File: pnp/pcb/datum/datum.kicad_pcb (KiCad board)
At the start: 2 copper layers, 80 x 35 mm, 9 parts

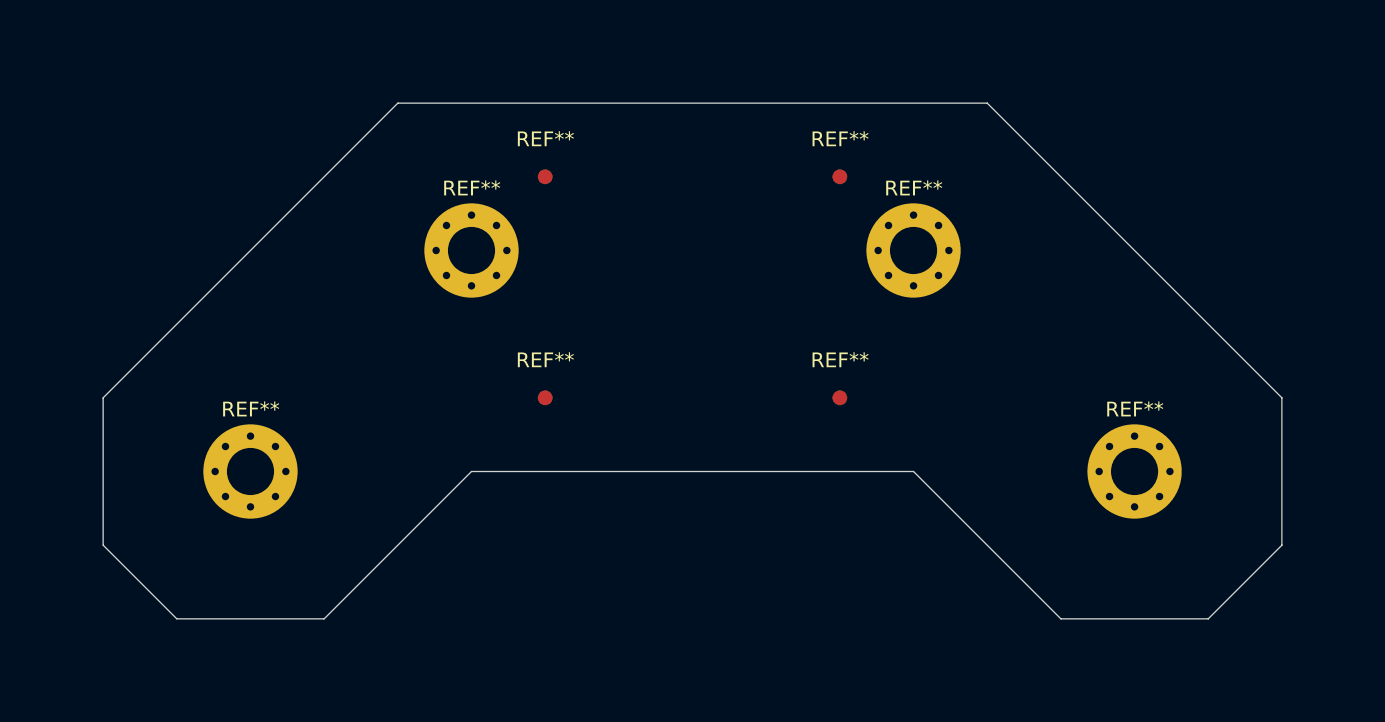
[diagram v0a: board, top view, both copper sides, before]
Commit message: got most of the top layer fids and features added
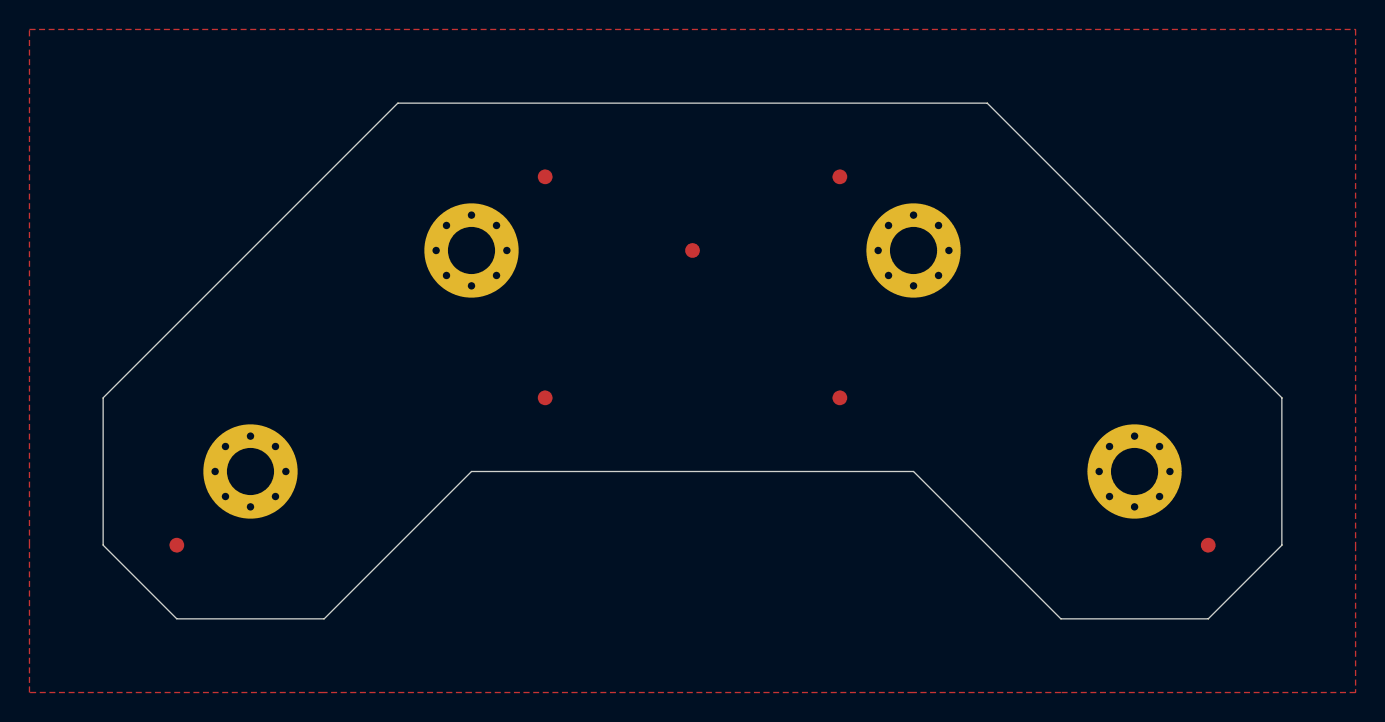
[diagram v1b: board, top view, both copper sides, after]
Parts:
- removed the REF** at (25.0, -25.0)
- removed the REF** at (55.0, -25.0)
- removed the REF** at (70.0, -10.0)
- removed the REF** at (10.0, -10.0)
- added H1: MountingHole_Pad, MountingHole:MountingHole_3.2mm_M3_Pad_Via, F.Cu at (25.0, -25.0)
- added H2: MountingHole_Pad, MountingHole:MountingHole_3.2mm_M3_Pad_Via, F.Cu at (10.0, -10.0)
- added H3: MountingHole_Pad, MountingHole:MountingHole_3.2mm_M3_Pad_Via, F.Cu at (70.0, -10.0)
- added H4: MountingHole_Pad, MountingHole:MountingHole_3.2mm_M3_Pad_Via, F.Cu at (55.0, -25.0)
- added REF**: Fiducial_1mm_Mask3mm, Fiducial:Fiducial_1mm_Mask3mm, F.Cu at (75.0, -5.00)
- added REF**: Fiducial_1mm_Mask3mm, Fiducial:Fiducial_1mm_Mask3mm, F.Cu at (5.00, -5.00)
- added REF**: Fiducial_1mm_Mask2mm, Fiducial:Fiducial_1mm_Mask2mm, F.Cu at (40.0, -25.0)
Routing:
- added copper zone on F.Cu, net GND

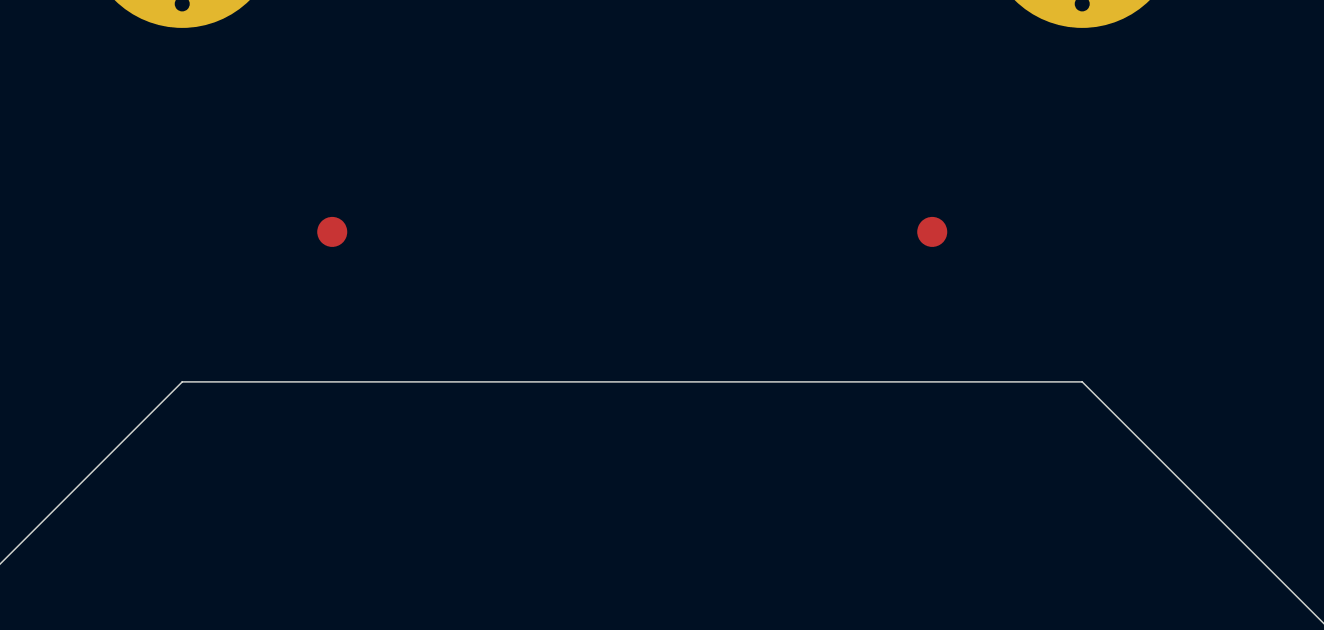
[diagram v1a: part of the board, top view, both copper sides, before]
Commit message: added footprints for ruler and dot grid for cam calibration, finalized board
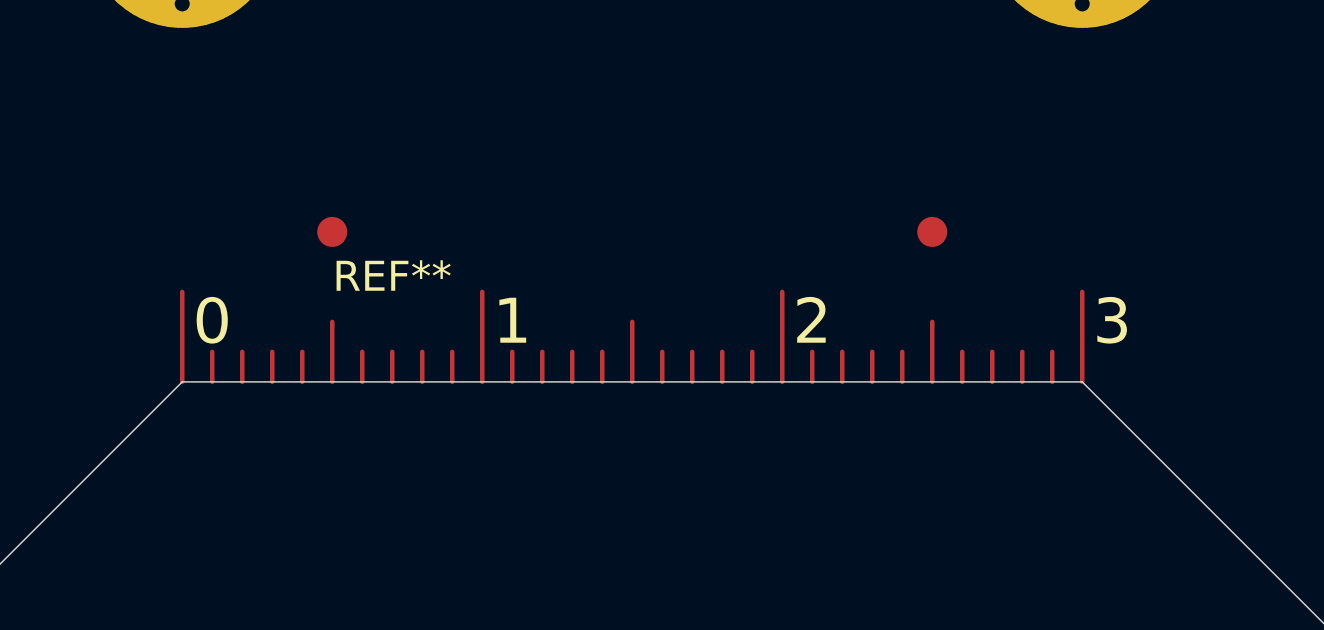
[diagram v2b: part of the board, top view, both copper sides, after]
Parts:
- added G***: LOGO, index:goblin, B.Cu at (17.0, -17.0)
- added G***: LOGO, index:cal-dot-grid, B.Cu at (40.0, -22.5)
- added REF**: Metric_Ruler_90mm, index:30mm-ruler, F.Cu at (25.0, -10.0)

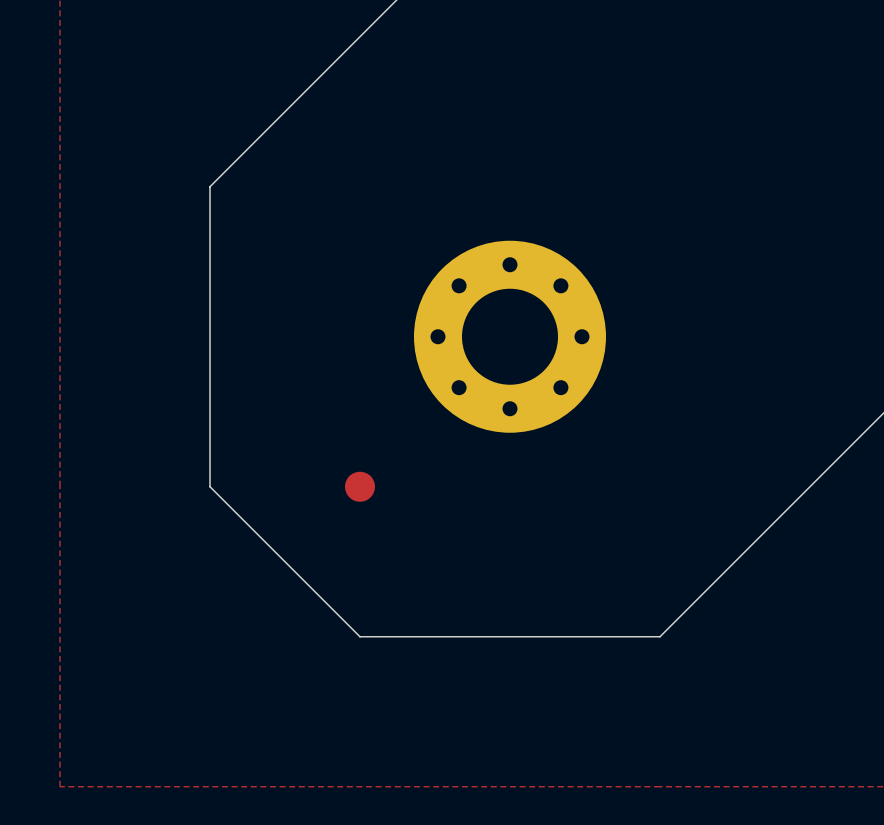
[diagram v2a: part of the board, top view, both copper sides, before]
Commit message: added castellated edges, and user drawing notes about them, along with notes about where to put the lot number
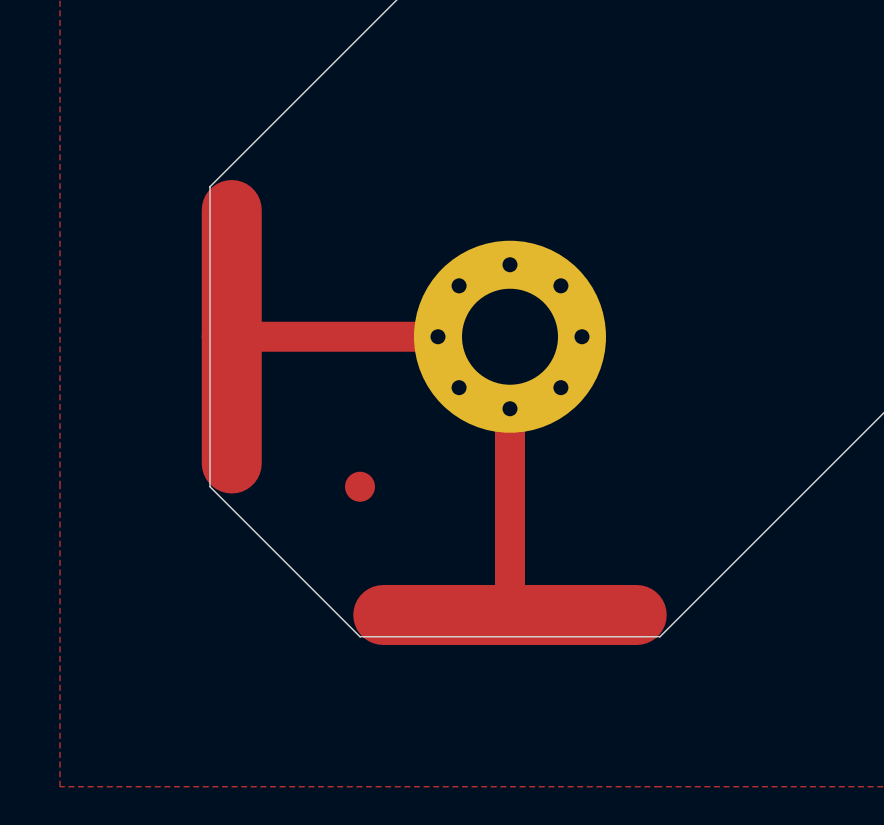
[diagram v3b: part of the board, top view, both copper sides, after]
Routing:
- net GND: track 0.00 -> 35.5 mm
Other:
- board text added: "Castellated along this flat edge"
- board text added: "Lot Number Here On Back Silkscreen"

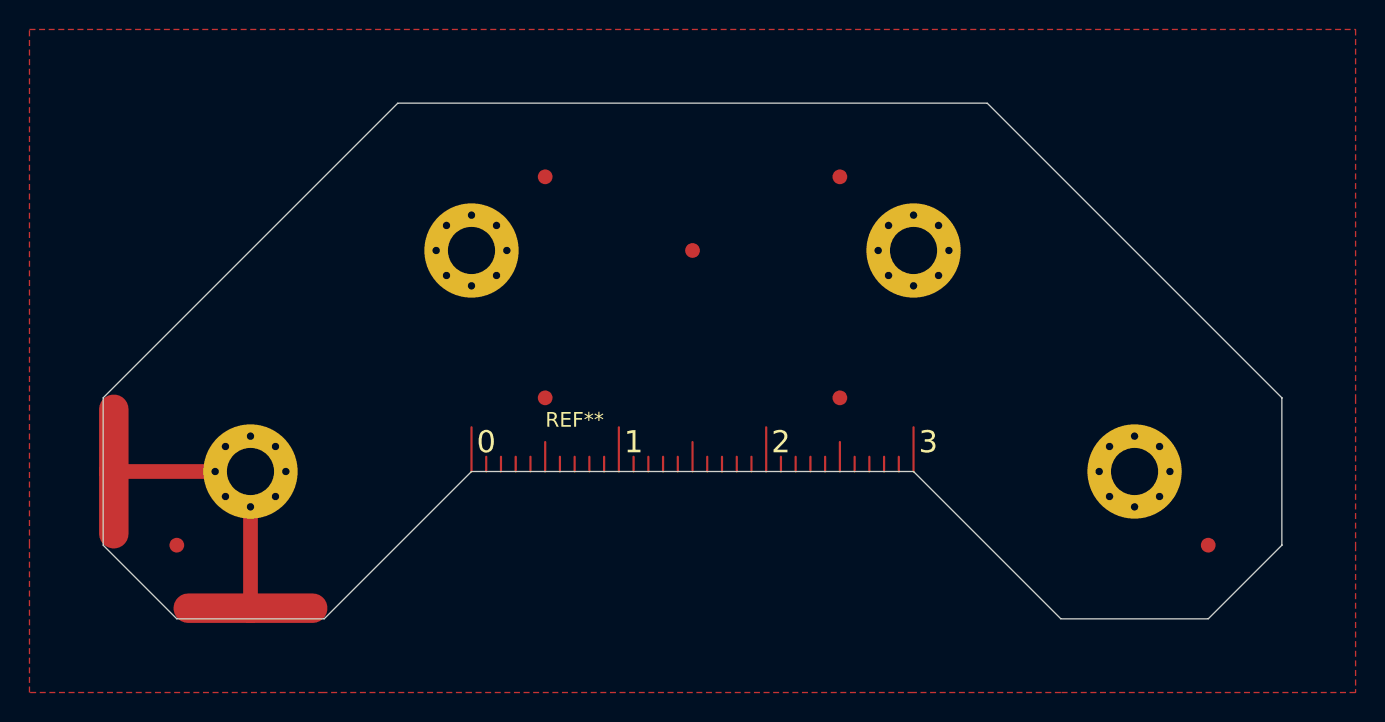
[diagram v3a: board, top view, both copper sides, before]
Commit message: made edge plating on the two internal diagonal faces, made solderable grounding pad on bottom face
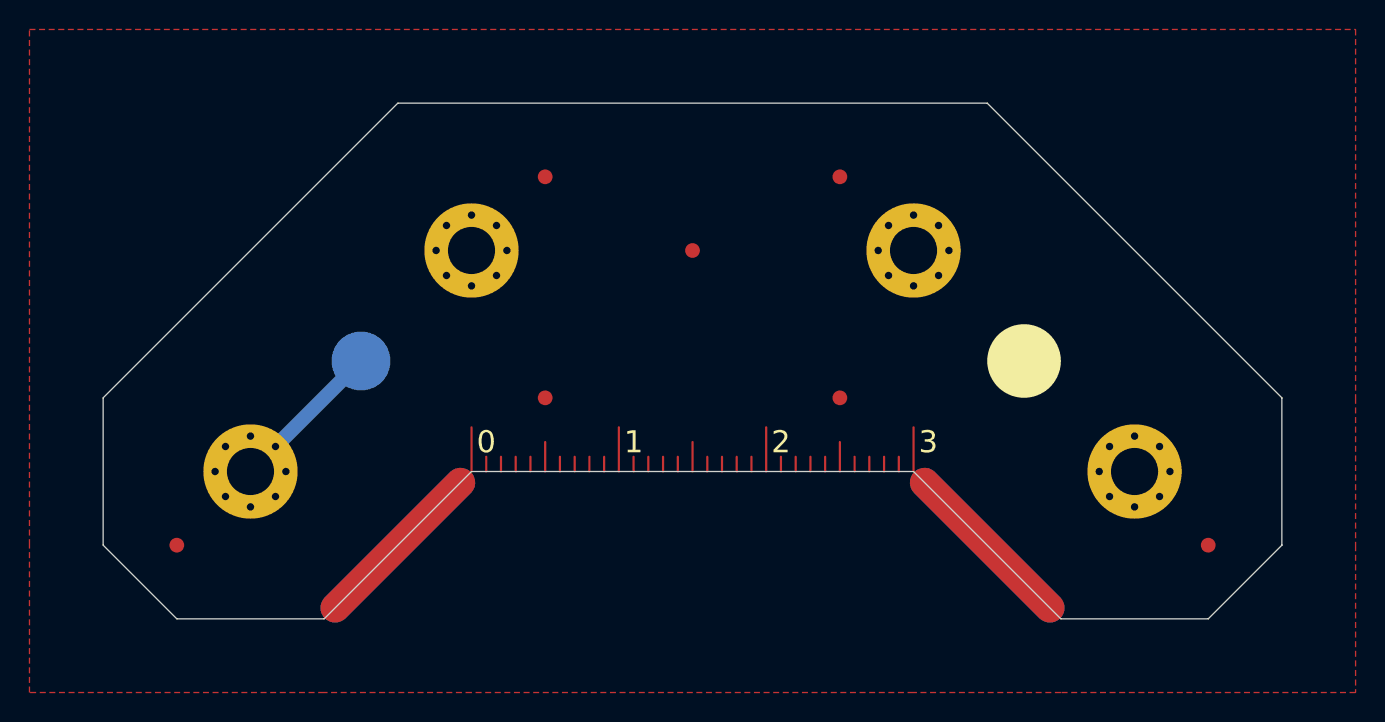
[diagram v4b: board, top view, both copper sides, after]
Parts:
- added TP1: TestPoint, TestPoint:TestPoint_Pad_D4.0mm, B.Cu at (17.5, -17.5)
- moved G*** 46.0 mm to (63.0, -17.0)
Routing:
- net (no net): track 0.00 -> 24.0 mm
- net GND: track 35.5 -> 34.6 mm
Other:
- board text added: "Plated along this flat edge"
- board text removed: "Castellated along this flat edge"
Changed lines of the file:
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@@
     (thickness 1.6)
     (drawings 33)
-    (tracks 6)
+    (tracks 5)
     (zones 0)
-    (modules 15)
+    (modules 16)
     (nets 2)
   )
@@
     (visible_elements FFFFFF7F)
     (pcbplotparams
-      (layerselection 0x010fc_ffffffff)
+      (layerselection 0x011fc_ffffffff)
       (usegerberextensions false)
       (usegerberattributes true)
@@
       (outputformat 1)
       (mirror false)
-      (drillshape 1)
+      (drillshape 0)
       (scaleselection 1)
-      (outputdirectory ""))
+      (outputdirectory "out/"))
   )
   (net 0 "")
@@
     (add_net GND)
   )
+  (module TestPoint:TestPoint_Pad_D4.0mm (layer B.Cu)
+    (at 17.5 -17.5)
+    (descr "SMD pad as test Point, diameter 4.0mm")
+    (tags "test point SMD pad")
+    (attr virtual)
+    (fp_text reference TP1 (at 0 2.898) (layer B.SilkS) hide
+      (effects (font (size 1 1) (thickness 0.15)) (justify mirror))
+    )
+    (fp_text value TestPoint (at 0 -3.1) (layer B.Fab)
+      (effects (font (size 1 1) (thickness 0.15)) (justify mirror))
+    )
+    (fp_circle (center 0 0) (end 2.5 0) (layer B.CrtYd) (width 0.05))
+    (fp_text user %R (at 0 2.9) (layer B.Fab)
+      (effects (font (size 1 1) (thickness 0.15)) (justify mirror))
+    )
+    (pad 1 smd circle (at 0 0) (size 4 4) (layers B.Cu B.Mask)
+      (net 1 GND))
+  )
   (module index:30mm-ruler (layer F.Cu)
     (at 25 -10)
-    (fp_text reference REF** (at 7.00024 -3.5005) (layer F.SilkS)
+    (fp_text reference REF** (at 7.00024 -3.5005) (layer F.SilkS) hide
       (effects (font (size 1 1) (thickness 0.15)))
     )
@@
   )
   (module index:goblin (layer B.Cu)
-    (at 17 -17 180)
+    (at 63 -17 180)
     (fp_text reference G*** (at 0 0) (layer B.SilkS) hide
       (effects (font (size 1.524 1.524) (thickness 0.3)) (justify mirror))
@@
       (net 1 GND))
   )
+  (gr_text "Plated along this flat edge" (at 19 -1.25 45) (layer Dwgs.User)
+    (effects (font (size 1 1) (thickness 0.15)))
+  )
   (gr_text "Lot Number Here\nOn Back Silkscreen" (at 70 -4.25) (layer Dwgs.User)
     (effects (font (size 1 1) (thickness 0.15)))
   )
-  (gr_text "Castellated along this flat edge" (at -1.25 -16.75 90) (layer Dwgs.User)
-    (effects (font (size 1 1) (thickness 0.15)))
-  )
-  (gr_text "Castellated along this flat edge" (at 17 1.5) (layer Dwgs.User)
+  (gr_text "Plated along this flat edge" (at 61 -1 -45) (layer Dwgs.User)
     (effects (font (size 1 1) (thickness 0.15)))
   )
@@
   (gr_line (start 52 -13) (end 28 -13) (layer B.Mask) (width 2))
   (gr_line (start 52 -32) (end 52 -13) (layer B.Mask) (width 2))
-  (gr_circle (center 62.5 -17.5) (end 63.75 -17.5) (layer F.Mask) (width 2.5))
+  (gr_circle (center 62.5 -17.5) (end 63.75 -17.5) (layer F.SilkS) (width 2.5))
   (gr_circle (center 17.5 -17.5) (end 18.75 -17.5) (layer F.Mask) (width 2.5))
   (gr_line (start 40 -30) (end 40 -29) (layer F.Mask) (width 0.15))
@@
   (gr_line (start 5 0) (end 0 -5) (layer Edge.Cuts) (width 0.05))
   (gr_line (start 5 0) (end 15 0) (layer Edge.Cuts) (width 0.05))
-  (segment (start 10 -0.72501) (end 5.77499 -0.72501) (width 2) (layer F.Cu) (net 1))
-  (segment (start 10 -0.72501) (end 14.22501 -0.72501) (width 2) (layer F.Cu) (net 1))
-  (segment (start 10 -10) (end 10 -0.72501) (width 1) (layer F.Cu) (net 1))
-  (segment (start 10 -10) (end 0.72501 -10) (width 1) (layer F.Cu) (net 1))
-  (segment (start 0.72501 -10) (end 0.72501 -14.22501) (width 2) (layer F.Cu) (net 1))
-  (segment (start 0.72501 -10) (end 0.72501 -5.77499) (width 2) (layer F.Cu) (net 1))
+  (segment (start 15.75 -0.75) (end 24.25 -9.25) (width 2) (layer B.Cu) (net 0))
+  (segment (start 64.25 -0.75) (end 55.75 -9.25) (width 2) (layer B.Cu) (net 0))
+  (segment (start 15.75 -0.75) (end 24.25 -9.25) (width 2) (layer F.Cu) (net 1))
+  (segment (start 64.25 -0.75) (end 55.75 -9.25) (width 2) (layer F.Cu) (net 1))
+  (segment (start 17.5 -17.5) (end 10 -10) (width 1) (layer B.Cu) (net 1))
   (zone (net 1) (net_name GND) (layer F.Cu) (hatch edge 0.508)
     (connect_pads (clearance 0.508))

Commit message: added pcb number and rev number to silkscreen
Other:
- board text added: "PCB-0004 REV00"
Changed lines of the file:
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@@
   (general
     (thickness 1.6)
-    (drawings 33)
+    (drawings 34)
     (tracks 5)
     (zones 0)
@@
       (net 1 GND))
   )
+  (gr_text "PCB-0004\nREV00" (at 70 -3.75) (layer B.SilkS)
+    (effects (font (size 1 1) (thickness 0.15)) (justify mirror))
+  )
   (gr_text "Plated along this flat edge" (at 19 -1.25 45) (layer Dwgs.User)
     (effects (font (size 1 1) (thickness 0.15)))
   )
-  (gr_text "Lot Number Here\nOn Back Silkscreen" (at 70 -4.25) (layer Dwgs.User)
+  (gr_text "Lot Number Here\nOn Back Silkscreen" (at 10 -4.5) (layer Dwgs.User)
     (effects (font (size 1 1) (thickness 0.15)))
   )

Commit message: Migrate Datum to KiCAD v6
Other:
- net class Default removed

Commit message: Update PCBs to KiCAD 8
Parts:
- renumbered G*** to G1, G*** to G2, G*** to G3
